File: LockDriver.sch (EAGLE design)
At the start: 18 parts, among them X1 M1, X2 M2, X3 VIN, X4 GND, X5 L, X6 U

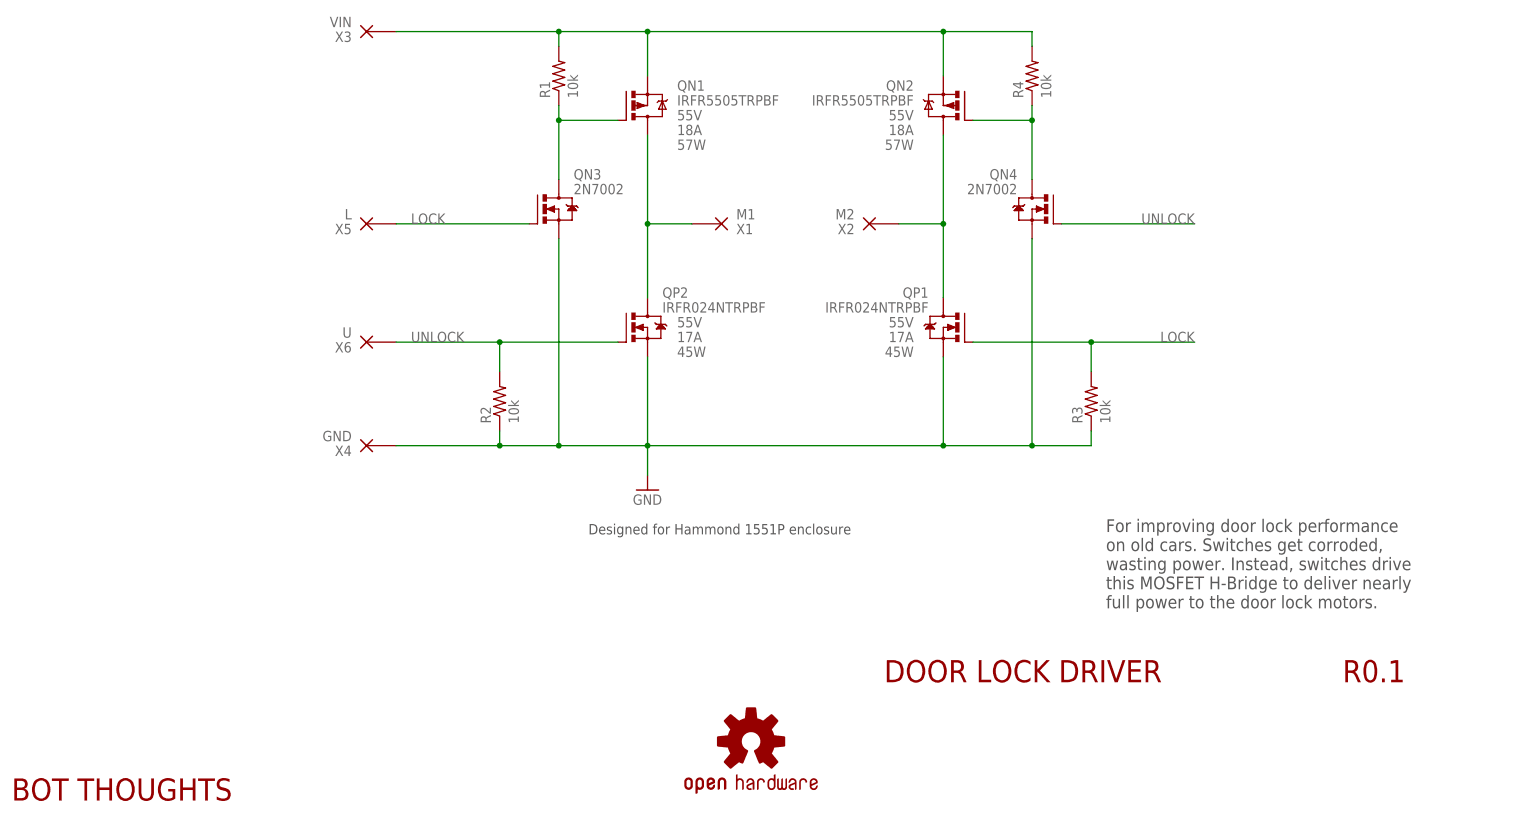
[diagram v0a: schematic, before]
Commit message: added diodes, changed wirepad sizes, layout changes
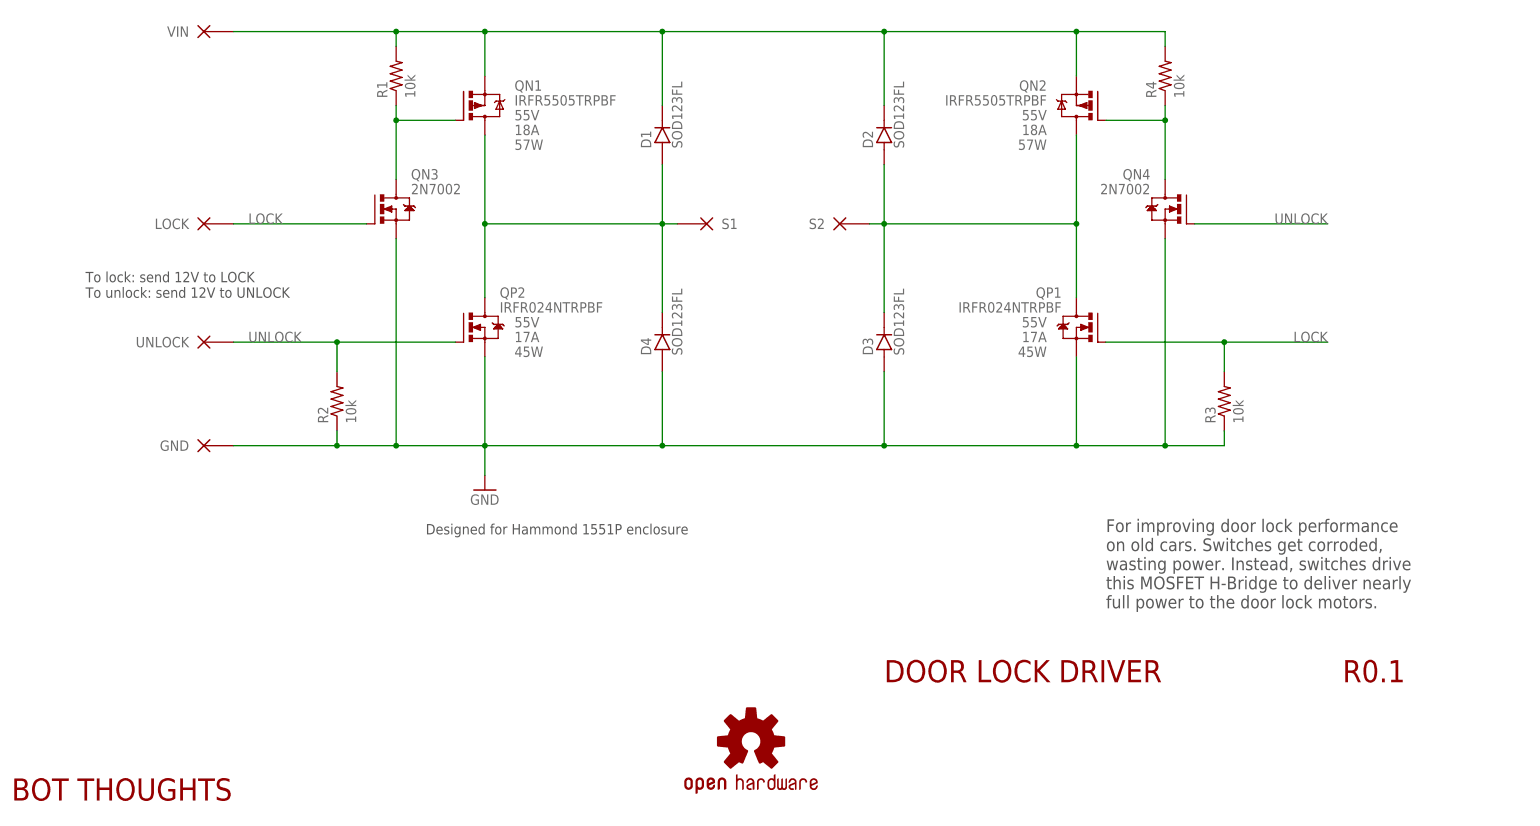
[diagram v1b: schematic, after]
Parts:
- added D1, D2, D3, D4: SOD123FL, bt_diode:DIODE_SOD123FL
- X1: value M1 -> S1; device bt_electromech:WIREPAD_18GA -> bt_electromech:WIREPAD_14GA
- X2: value M2 -> S2; device bt_electromech:WIREPAD_18GA -> bt_electromech:WIREPAD_14GA
- X3, X4: device bt_electromech:WIREPAD_14GA -> bt_electromech:WIREPAD_12GA
- X5: value L -> LOCK
- X6: value U -> UNLOCK
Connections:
- net 12V: now also D1.C, D2.C
- net GND: now also D3.A, D4.A
- net M1: now also D1.A, D4.C
- net M2: now also D2.A, D3.C
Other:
- note added: "To lock: send 12V to LOCK To unlock: send 12V to UNLOCK"
- moved on the sheet: QN1, QN2, QN3, QN4, QP1, QP2, R1, R2, R3, R4
